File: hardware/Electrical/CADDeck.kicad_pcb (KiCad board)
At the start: 2 copper layers, 129 x 82.1 mm, 36 parts, among them J1 Conn_01x05_Socket, J4 Conn_01x04_Socket, J5 Conn_01x10_Socket, SW1 SW_Push, SW10 SW_Push, SW2 SW_Push, SW3 SW_Push, SW4 SW_Push, SW5 SW_Push, SW6 SW_Push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

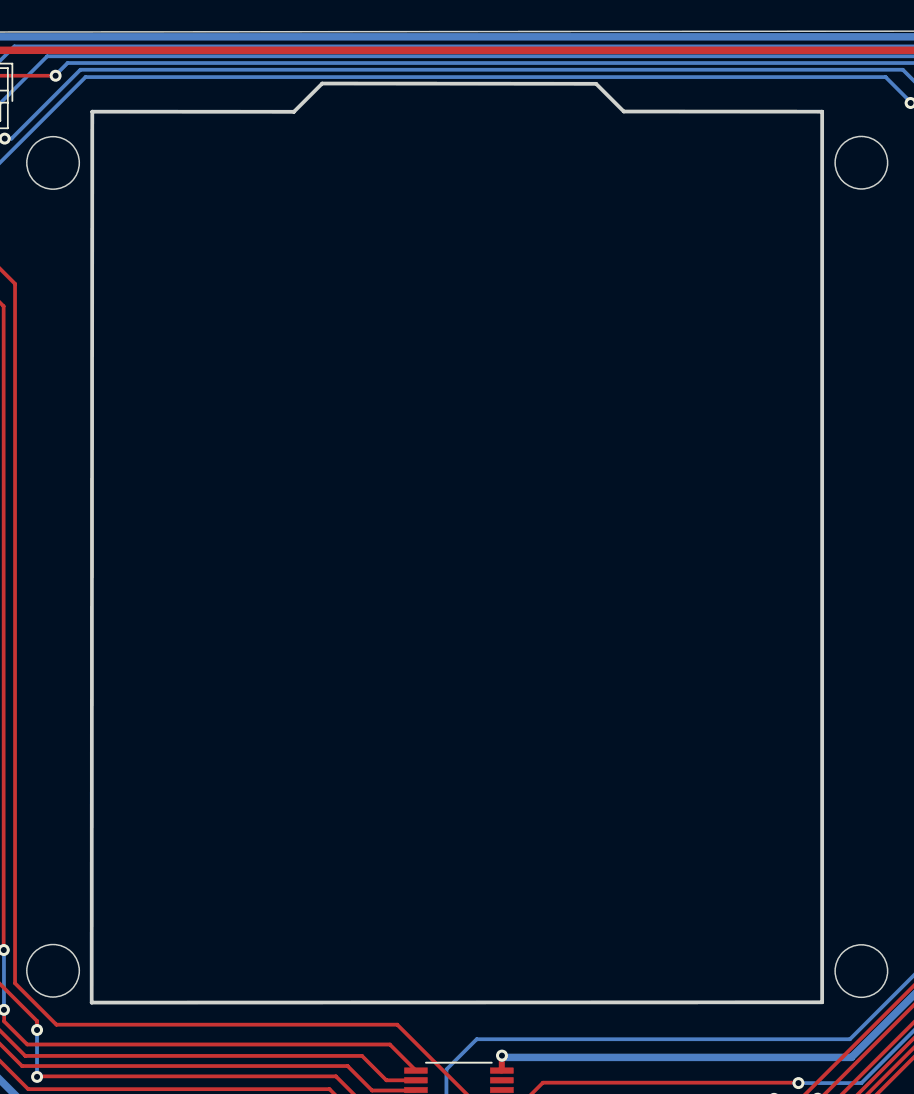
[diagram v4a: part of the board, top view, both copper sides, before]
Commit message: MX_LED_Beleuchtung hinzugefügt
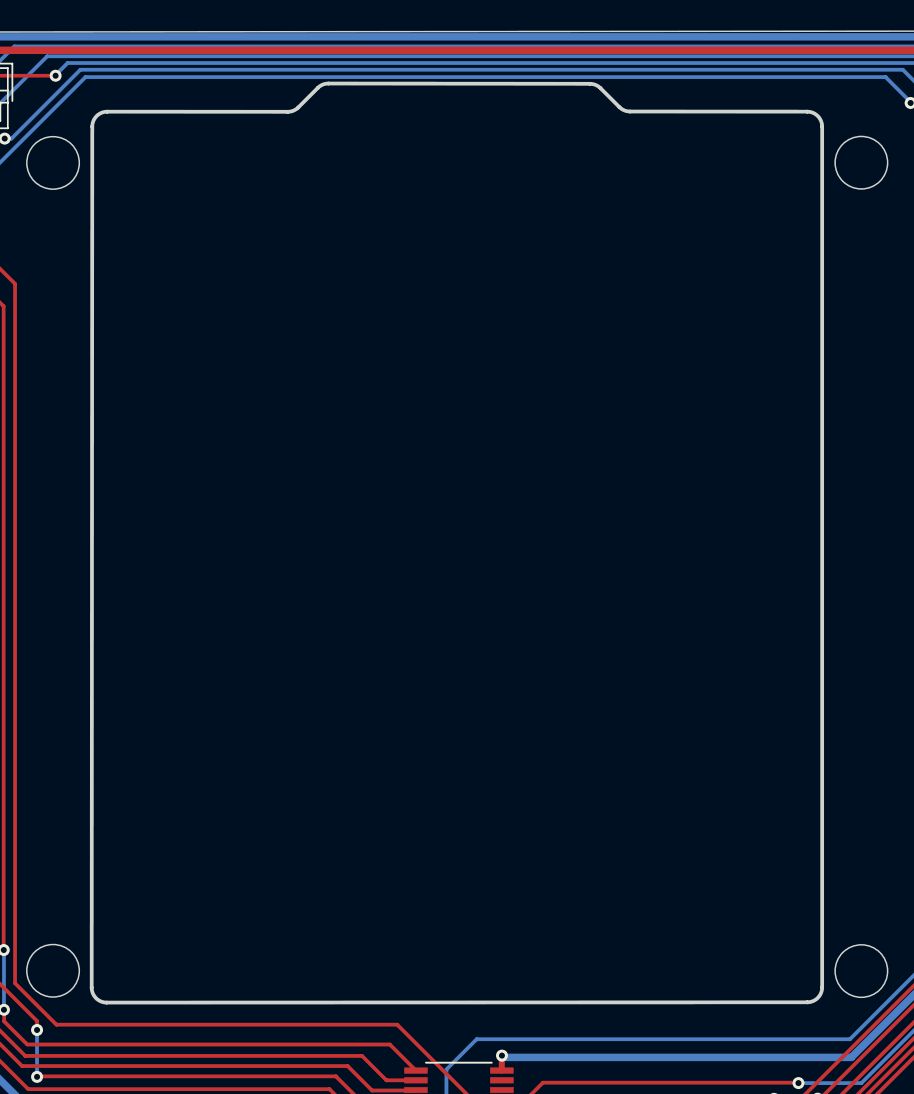
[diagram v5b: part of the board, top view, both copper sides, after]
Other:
- outline, holes or cut-outs redrawn
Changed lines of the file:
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@@
         (effects (font (size 1 1) (thickness 0.15)))
     )
-    (fp_text value "PCF8575PWE4" (at -0.53 -5.955) (layer "F.Fab")
+    (fp_text value "PCF8575PWE4" (at -2.591 6.773) (layer "F.Fab")
         (effects (font (size 1 1) (thickness 0.15)))
     )
@@
     (pad "24" smd roundrect (at 2.87 -3.575 180) (size 1.57 0.41) (layers "F.Cu" "F.Paste" "F.Mask") (roundrect_rratio 0.05)
       (net 1 "+3.3V") (pinfunction "VCC") (pintype "power_in"))
+    (model ":KICAD7_3DMODEL_DIR:Eigene.3dshapes/PCF8575PWE4.step"
+      (offset (xyz 0 0 0))
+      (scale (xyz 1 1 1))
+      (rotate (xyz 90 180 180))
+    )
   )
   (footprint "Connector_JST:JST_EH_B5B-EH-A_1x05_P2.50mm_Vertical" (layer "F.Cu")
@@
   (gr_line (start 87.79 85.43) (end 88.27 89.39)
     (stroke (width 0.1) (type solid)) (layer "Edge.Cuts"))
-  (gr_line (start 127.6 62.05) (end 127.56 121.57)
+  (gr_line (start 127.599328 63.05007) (end 127.560673 120.568918)
     (stroke (width 0.25) (type solid)) (layer "Edge.Cuts"))
   (gr_line (start 197.42 128.54) (end 195.51 130.93)
     (stroke (width 0.1) (type default)) (layer "Edge.Cuts"))
-  (gr_line (start 163.11 62.04) (end 161.26 60.19)
+  (gr_line (start 162.817419 61.747419) (end 161.55244 60.48244)
     (stroke (width 0.25) (type solid)) (layer "Edge.Cuts"))
   (gr_line (start 214.61 95.72) (end 215.34 92.29)
@@
   (gr_circle (center 178.98 65.46) (end 180.733853 65.46)
     (stroke (width 0.1) (type solid)) (fill solid) (layer "Edge.Cuts"))
-  (gr_line (start 142.96 60.17) (end 141.07 62.06)
+  (gr_line (start 142.666654 60.463346) (end 141.363201 61.766799)
     (stroke (width 0.25) (type solid)) (layer "Edge.Cuts"))
+  (gr_arc (start 128.561083 121.56959) (mid 127.853474 121.276604) (end 127.560673 120.568918)
+    (stroke (width 0.25) (type default)) (layer "Edge.Cuts"))
   (gr_line (start 212.58 102.96) (end 213.09 101.605)
     (stroke (width 0.1) (type solid)) (layer "Edge.Cuts"))
@@
   (gr_line (start 206.6 116.26) (end 208.03 113.7)
     (stroke (width 0.1) (type solid)) (layer "Edge.Cuts"))
+  (gr_arc (start 175.360755 62.049246) (mid 176.067358 62.342409) (end 176.36 63.049246)
+    (stroke (width 0.25) (type default)) (layer "Edge.Cuts"))
   (gr_line (start 87.4 56.76) (end 87.42 81.54)
     (stroke (width 0.1) (type solid)) (layer "Edge.Cuts"))
@@
   (gr_line (start 90.62 101.73) (end 92.49 107.33)
     (stroke (width 0.1) (type solid)) (layer "Edge.Cuts"))
-  (gr_line (start 141.07 62.06) (end 127.6 62.05)
+  (gr_line (start 140.655352 62.059692) (end 128.60007 62.050742)
     (stroke (width 0.25) (type solid)) (layer "Edge.Cuts"))
   (gr_line (start 216.36 81.22) (end 216.36 56.64)
@@
   (gr_line (start 197.42 128.54) (end 201.11 124.33)
     (stroke (width 0.1) (type solid)) (layer "Edge.Cuts"))
-  (gr_line (start 127.56 121.57) (end 176.36 121.55)
+  (gr_line (start 128.561083 121.56959) (end 175.36041 121.55041)
     (stroke (width 0.25) (type solid)) (layer "Edge.Cuts"))
   (gr_line (start 95.82 114.57) (end 97.37 117.34)
     (stroke (width 0.1) (type solid)) (layer "Edge.Cuts"))
+  (gr_arc (start 127.599328 63.05007) (mid 127.892708 62.343118) (end 128.60007 62.050742)
+    (stroke (width 0.25) (type default)) (layer "Edge.Cuts"))
+  (gr_arc (start 160.846427 60.189548) (mid 161.228512 60.265891) (end 161.55244 60.48244)
+    (stroke (width 0.25) (type default)) (layer "Edge.Cuts"))
   (gr_line (start 208.03 113.7) (end 209.75 110.08)
     (stroke (width 0.1) (type solid)) (layer "Edge.Cuts"))
   (gr_circle (center 113.54 127.19) (end 119.55173 127.19)
     (stroke (width 0.1) (type solid)) (fill solid) (layer "Edge.Cuts"))
+  (gr_arc (start 163.523771 62.040312) (mid 163.141488 61.964056) (end 162.817419 61.747419)
+    (stroke (width 0.25) (type default)) (layer "Edge.Cuts"))
+  (gr_arc (start 176.36 120.55041) (mid 176.067252 121.257372) (end 175.36041 121.55041)
+    (stroke (width 0.25) (type default)) (layer "Edge.Cuts"))
   (gr_line (start 211.12 106.8) (end 212.58 102.96)
     (stroke (width 0.1) (type solid)) (layer "Edge.Cuts"))
@@
   (gr_line (start 103.8 126.12) (end 104.83 127.25)
     (stroke (width 0.1) (type solid)) (layer "Edge.Cuts"))
-  (gr_line (start 176.36 121.55) (end 176.36 62.05)
+  (gr_line (start 176.36 120.55041) (end 176.36 63.049246)
     (stroke (width 0.25) (type solid)) (layer "Edge.Cuts"))
-  (gr_line (start 176.36 62.05) (end 163.11 62.04)
+  (gr_line (start 175.360755 62.049246) (end 163.523771 62.040312)
     (stroke (width 0.25) (type solid)) (layer "Edge.Cuts"))
   (gr_line (start 117.2 138.63) (end 117.34 138.72)
     (stroke (width 0.1) (type default)) (layer "Edge.Cuts"))
-  (gr_line (start 161.26 60.19) (end 142.96 60.17)
+  (gr_arc (start 141.363201 61.766799) (mid 141.038435 61.983714) (end 140.655352 62.059692)
+    (stroke (width 0.25) (type default)) (layer "Edge.Cuts"))
+  (gr_line (start 160.846427 60.189548) (end 143.374854 60.170453)
     (stroke (width 0.25) (type solid)) (layer "Edge.Cuts"))
   (gr_line (start 114.02 136.24) (end 115.81 137.67)
@@
   (gr_line (start 189.86 136.06) (end 187.11 138.1)
     (stroke (width 0.1) (type default)) (layer "Edge.Cuts"))
+  (gr_arc (start 142.666654 60.463346) (mid 142.991582 60.246364) (end 143.374854 60.170453)
+    (stroke (width 0.25) (type default)) (layer "Edge.Cuts"))
   (gr_text "AFUDirk\nCADDeck 10 Buttons" (at 122.58 136.713) (layer "F.Cu")
     (effects (font (size 2 2) (thickness 0.4) bold) (justify left bottom))

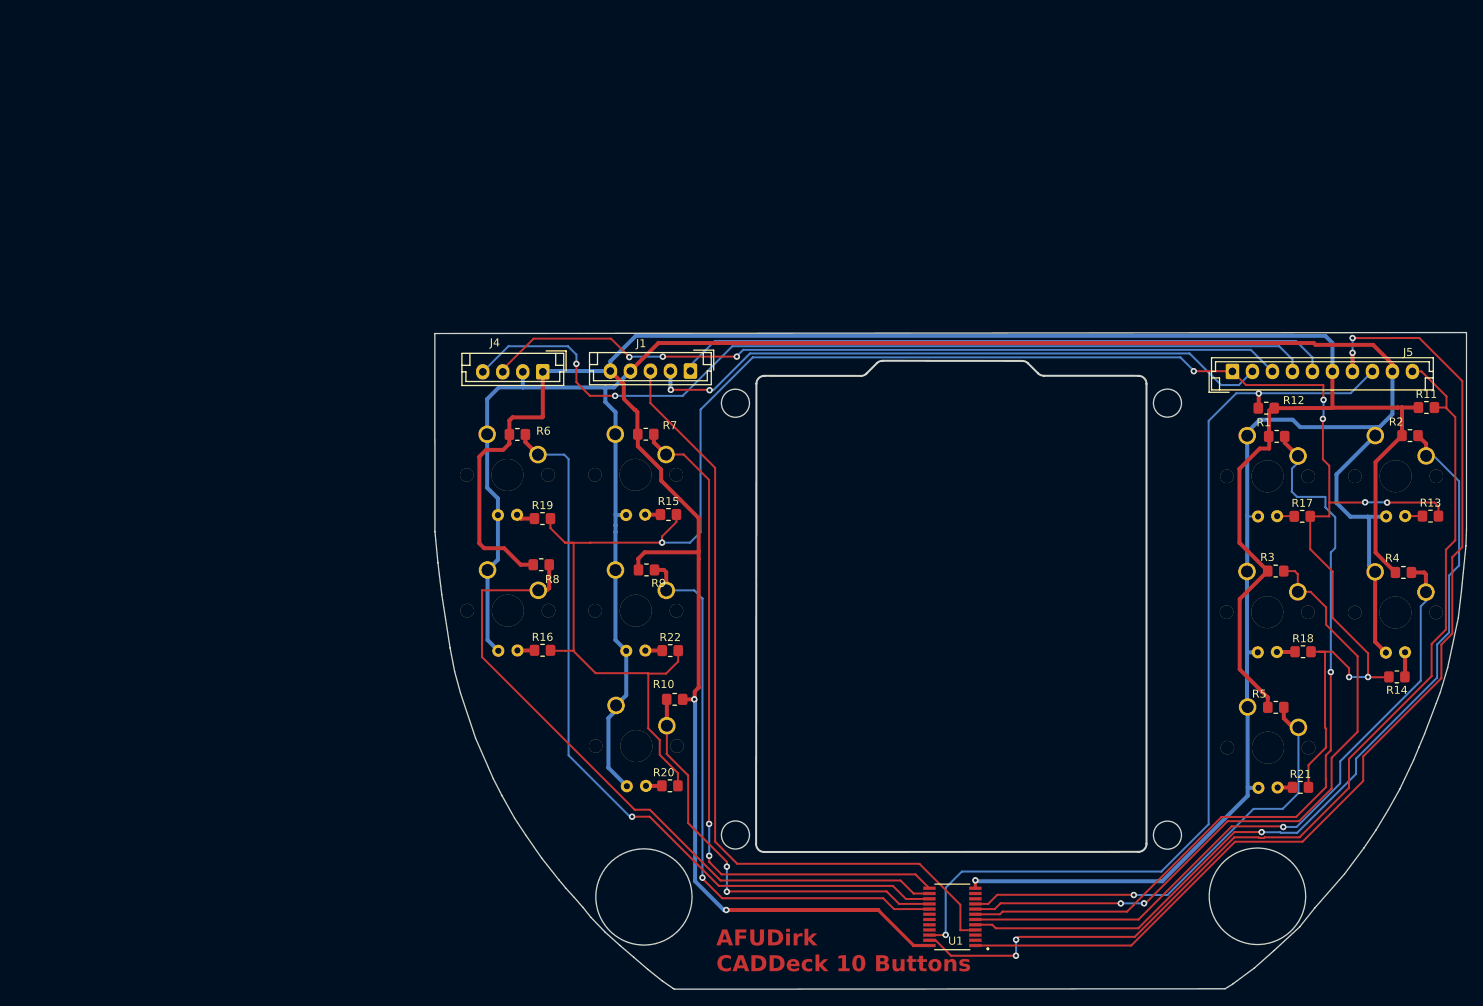
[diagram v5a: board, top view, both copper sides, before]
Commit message: Board Transistor eingefügt
Für LED Beleuchtung und Leiterbahnen angepasst.
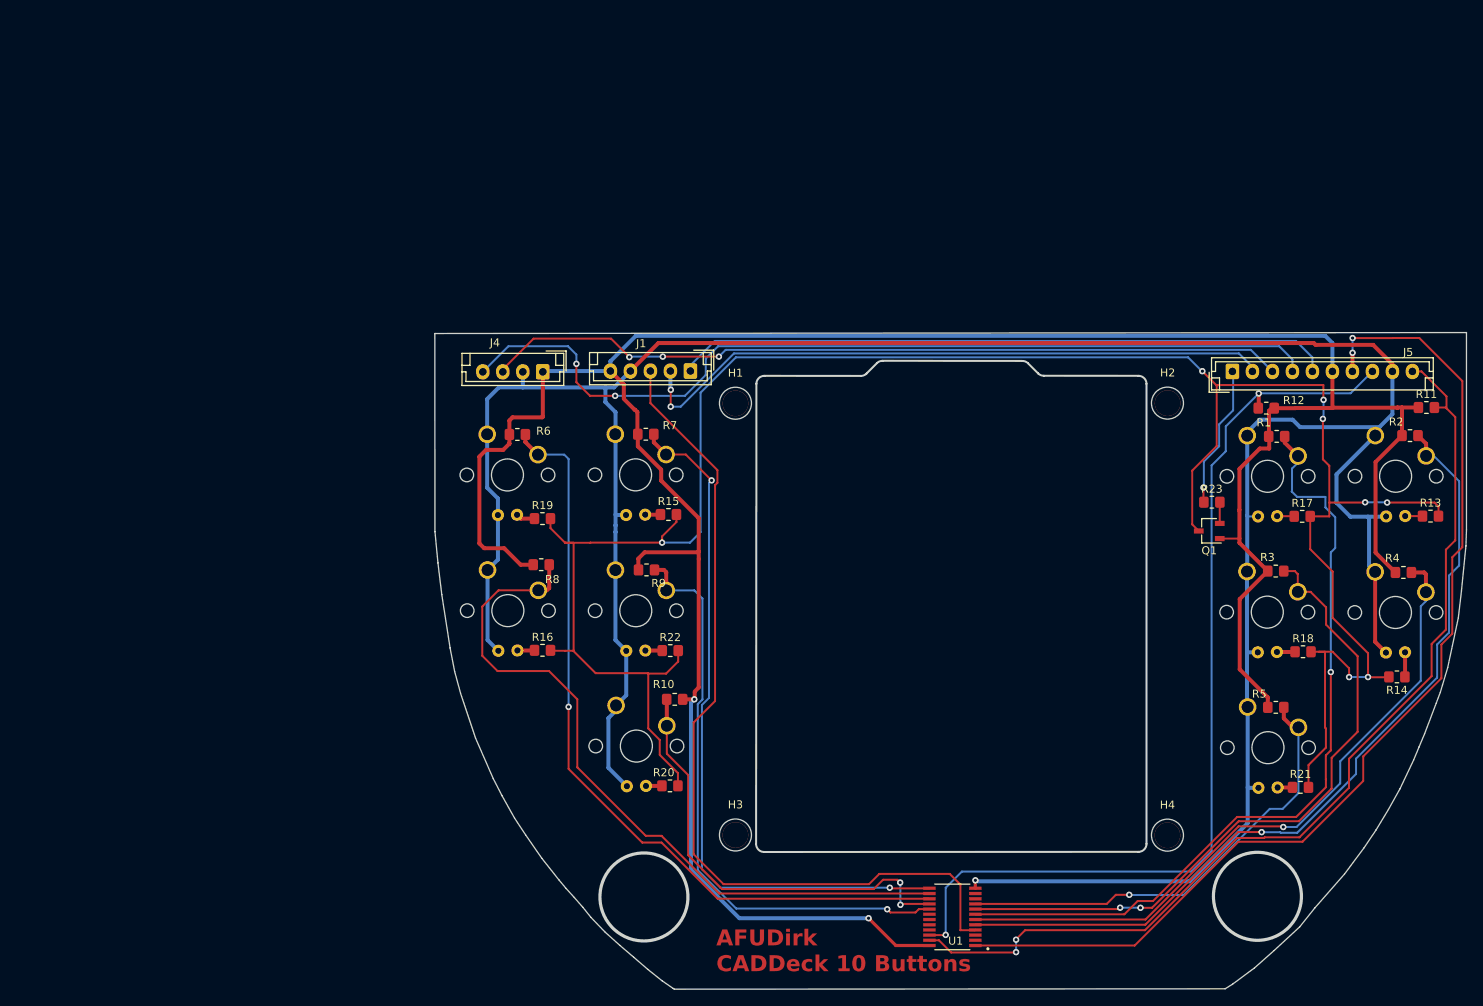
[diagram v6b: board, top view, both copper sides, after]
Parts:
- added H1: Bohrung Joy, MountingHole:MountingHole_3.2mm_M3_DIN965, F.Cu at (125.0, 65.5)
- added H2: Bohrung Joy, MountingHole:MountingHole_3.2mm_M3_DIN965, F.Cu at (179.0, 65.5)
- added H3: Bohrung Joy, MountingHole:MountingHole_3.2mm_M3_DIN965, F.Cu at (125.0, 119.5)
- added H4: Bohrung Joy, MountingHole:MountingHole_3.2mm_M3_DIN965, F.Cu at (179.0, 119.5)
- added Q1: 2N2222, Package_TO_SOT_SMD:TSOT-23, F.Cu at (184.2, 81.4)
- added R23: 1k, Resistor_SMD:R_0805_2012Metric_Pad1.20x1.40mm_HandSolder, F.Cu at (184.5, 77.8)
- SW1, SW10, SW2, SW3, SW4, SW5, SW6, SW7, SW8, SW9: footprint Button_MX_LED:SW_Cherry_MX_LED_PCB -> Cherry_MX_LED:Cherry_MX_LED
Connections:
- R13 pad 2: Net-(J5-Pin_1) -> Net-(Q1-C)
- R14 pad 2: Net-(J5-Pin_1) -> Net-(Q1-C)
- R15 pad 2: Net-(J5-Pin_1) -> Net-(Q1-C)
- R16 pad 2: Net-(J5-Pin_1) -> Net-(Q1-C)
- R17 pad 2: Net-(J5-Pin_1) -> Net-(Q1-C)
- R18 pad 2: Net-(J5-Pin_1) -> Net-(Q1-C)
- R19 pad 2: Net-(J5-Pin_1) -> Net-(Q1-C)
- R20 pad 2: Net-(J5-Pin_1) -> Net-(Q1-C)
- R21 pad 2: Net-(J5-Pin_1) -> Net-(Q1-C)
- R22 pad 2: Net-(J5-Pin_1) -> Net-(Q1-C)
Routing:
- net Net-(Q1-C): track 0.00 -> 280.9 mm, vias 0 -> 8
- net Net-(J5-Pin_1): track 259.8 -> 18.0 mm, vias 8 -> 1
- net Net-(J1-Pin_3): track 101.2 -> 108.7 mm
- net Net-(U1-P11): track 87.9 -> 91.6 mm
- net Net-(U1-P13): track 53.3 -> 55.9 mm
- net Net-(Q1-B): track 0.00 -> 2.65 mm
- net +3.3V: track 343.3 -> 345.9 mm
- net Net-(U1-P10): track 86.5 -> 88.7 mm
- net GND: track 356.5 -> 358.5 mm
- net Net-(J1-Pin_2): track 79.3 -> 81.2 mm
- net Net-(J4-Pin_4): track 111.9 -> 113.1 mm
- net Net-(U1-P12): track 96.8 -> 97.8 mm
- net Net-(J5-Pin_10): track 125.1 -> 124.4 mm
- net Net-(U1-P14): track 72.9 -> 73.5 mm
- net Net-(J5-Pin_8): track 119.4 -> 120.0 mm
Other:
- outline, holes or cut-outs redrawn

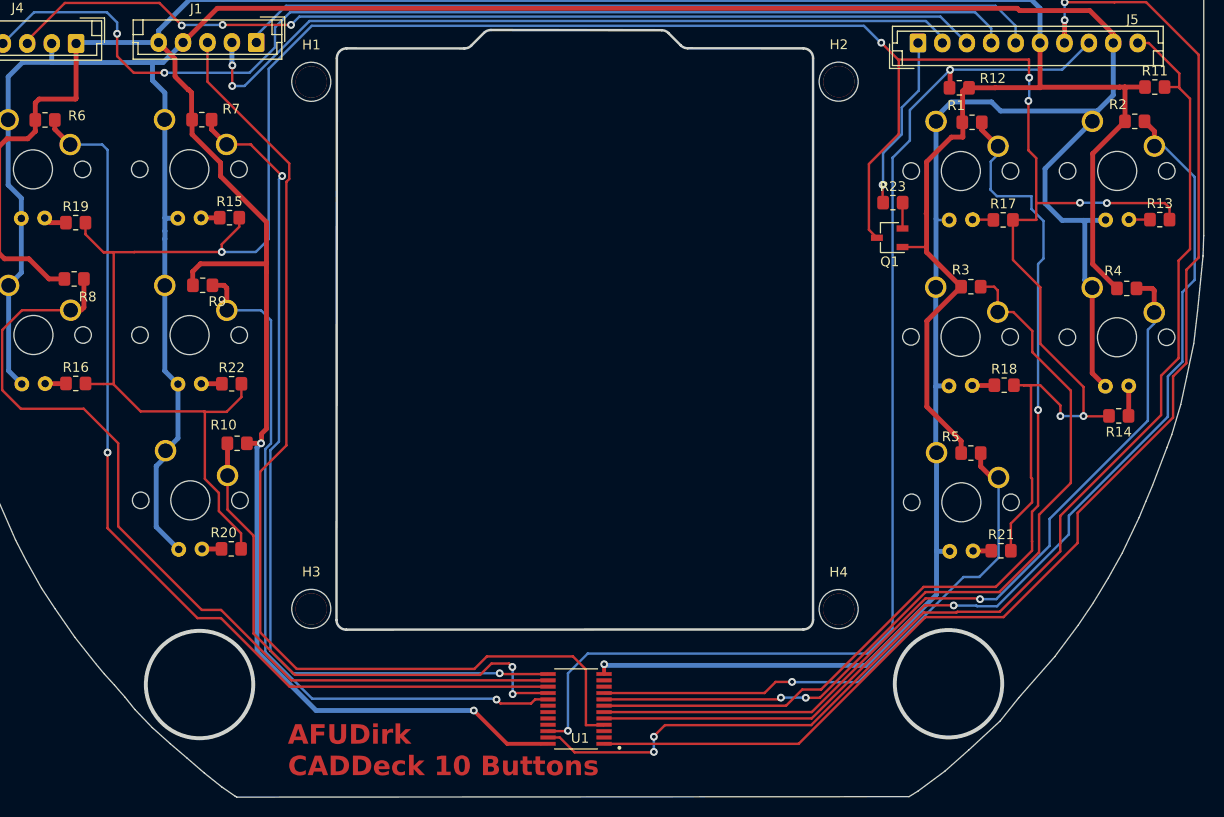
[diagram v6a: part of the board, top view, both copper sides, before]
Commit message: Platine optimiert
und Gerberdateien aktualisiert.
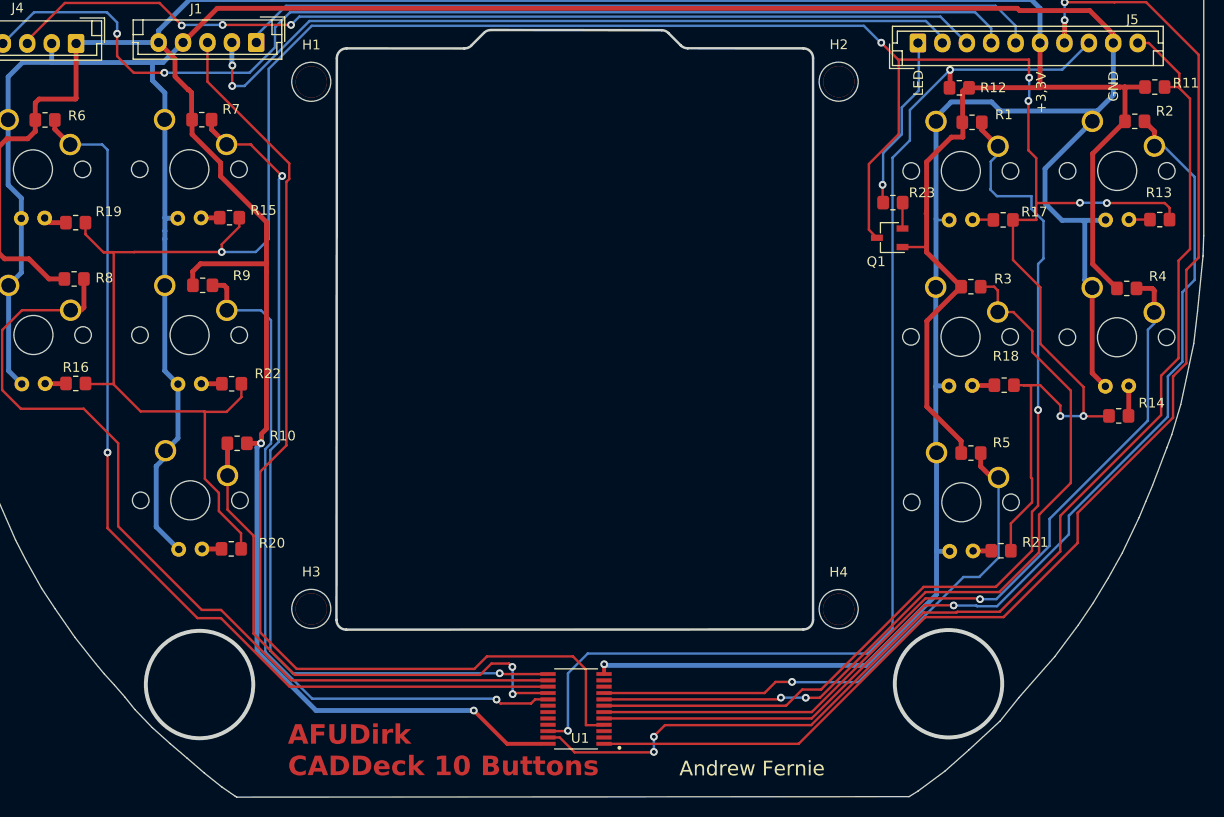
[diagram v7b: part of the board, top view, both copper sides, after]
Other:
- board text added: "+3,3V"
- board text added: "Andrew Fernie"
- board text added: "GND"
- board text added: "LED"
